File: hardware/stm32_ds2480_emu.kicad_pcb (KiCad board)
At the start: 2 copper layers, 33 x 14 mm, 28 parts, among them J1 OW, J2 USB_A, J3 SWD, Q1 SI2302CDS, U1 USBLC6-2SC6, U2 STM32F042F6Px, U3 AP2204K-3.3

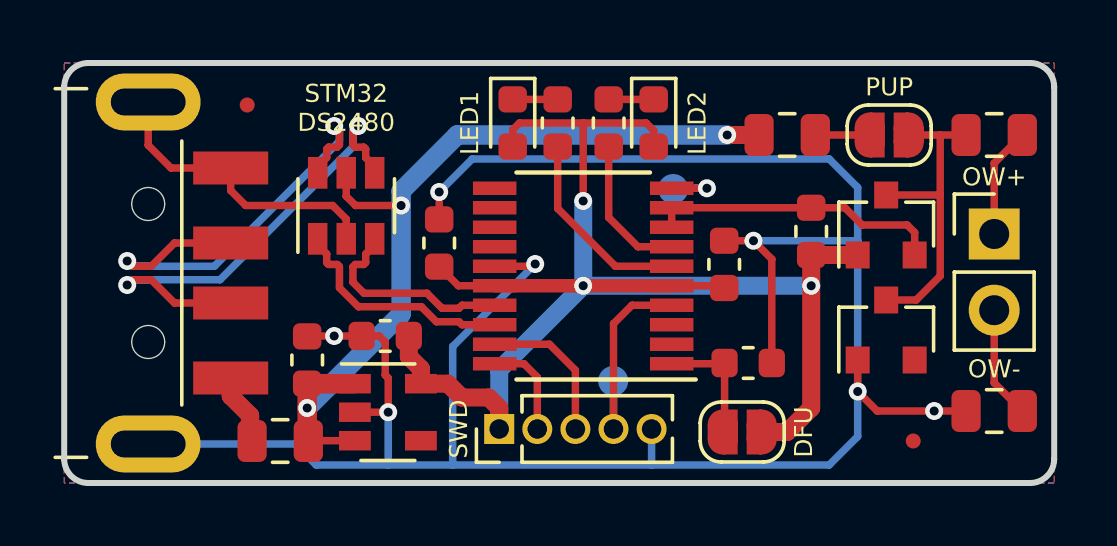
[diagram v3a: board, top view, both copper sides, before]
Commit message: Started using KiKit for the panelization.
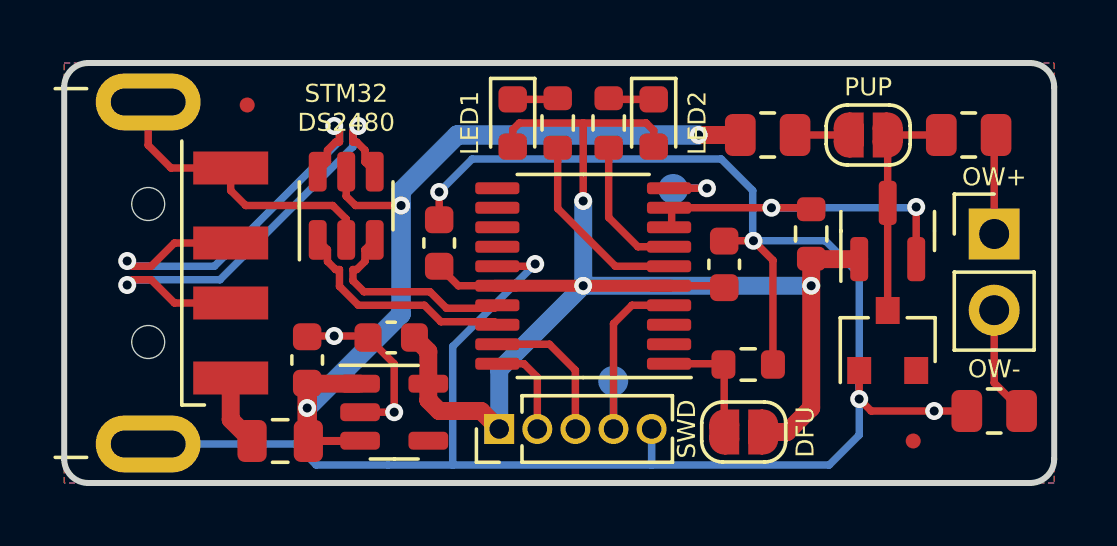
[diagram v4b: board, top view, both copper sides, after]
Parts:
- moved R4 0.85 mm to (170.9, 102.2)
- moved JP1 0.70 mm to (167.6, 102.2)
- moved R3 0.65 mm to (164.2, 102.2)
- moved D3 0.35 mm to (168.2, 109.0)
- moved U3 0.21 mm to (151.8, 111.4)
- moved Q1 0.21 mm to (168.2, 105.4)
- moved C3 0.21 mm to (151.7, 109.0)
- moved R5 0.09 mm to (165.7, 105.5)
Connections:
- U2 pad 11: Net-(U2-Pad11) -> unconnected-(U2-Pad11)
- U2 pad 12: Net-(U2-Pad12) -> unconnected-(U2-Pad12)
- U2 pad 13: Net-(U2-Pad13) -> unconnected-(U2-Pad13)
- U2 pad 14: Net-(U2-Pad14) -> unconnected-(U2-Pad14)
- U2 pad 2: Net-(U2-Pad2) -> unconnected-(U2-Pad2)
- U2 pad 3: Net-(U2-Pad3) -> unconnected-(U2-Pad3)
- U3 pad 4: Net-(U3-Pad4) -> unconnected-(U3-Pad4)
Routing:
- net GND: track 90.6 -> 84.6 mm
- net Net-(D3-Pad1): track 10.5 -> 7.64 mm
- net /OW-3V3: track 9.84 -> 11.9 mm, vias 0 -> 2
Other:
- net class Default removed
- net class POWER removed
